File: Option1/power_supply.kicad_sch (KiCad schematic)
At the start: 36 parts, among them U201 U7812-500, U202 K7805-500R2_C909663, U203 SY8089AAAC, U204 SY8089AAAC

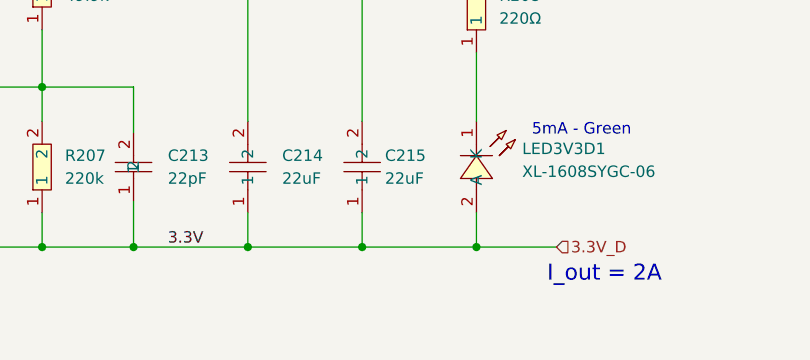
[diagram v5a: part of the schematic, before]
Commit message: 3V3 für Display hinzugefügt und gelayoutet, Brücke zwischen Display und Std 3V3 hinzugefügt in Schaltplan und Platine
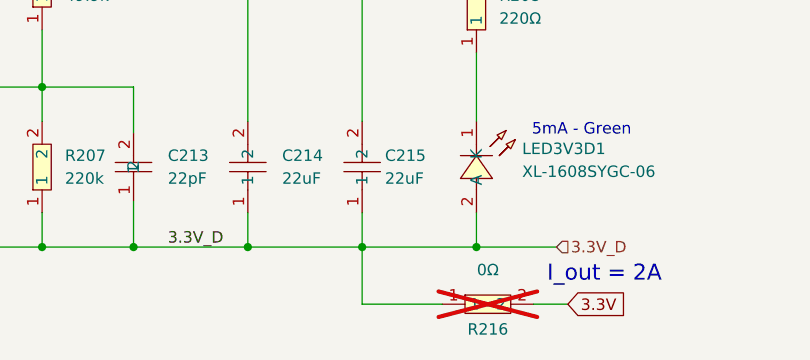
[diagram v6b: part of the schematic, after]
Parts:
- added R216: 0Ω, easyeda2kicad:R0603, symbol easyeda2kicad:0603WAF0000T5E
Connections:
- net 3.3V: now also R216.2; no longer C213.1, C214.1, C215.1, L202.2, LED3V3D1.2 (A), R207.1
- new net 3.3V_D: C213.1, C214.1, C215.1, L202.2, LED3V3D1.2 (A), R207.1, R216.1
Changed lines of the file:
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@@
+	(wire
+		(pts
+			(xy 236.22 116.84) (xy 227.33 116.84)
+		)
+		(stroke
+			(width 0)
+			(type default)
+		)
+	)
 	(wire
 		(pts
@@
 	(wire
 		(pts
+			(xy 227.33 116.84) (xy 227.33 110.49)
+		)
+		(stroke
+			(width 0)
+			(type default)
+		)
+	)
+	(wire
+		(pts
 			(xy 227.33 59.69) (xy 240.03 59.69)
 		)
@@
 		(pts
 			(xy 86.36 77.47) (xy 93.98 77.47)
+		)
+		(stroke
+			(width 0)
+			(type default)
+		)
+	)
+	(wire
+		(pts
+			(xy 246.38 116.84) (xy 250.19 116.84)
 		)
 		(stroke
@@
 		)
 	)
-	(label "3.3V"
+	(label "3.3V_D"
 		(at 205.74 110.49 0)
 		(effects
@@
 		(property "Intersheetrefs" "${INTERSHEET_REFS}"
 			(at 138.9357 57.15 0)
+			(effects
+				(font
+					(size 1.27 1.27)
+				)
+				(justify left)
+				(hide yes)
+			)
+		)
+	)
+	(global_label "3.3V"
+		(shape input)
+		(at 250.19 116.84 0)
+		(fields_autoplaced yes)
+		(effects
+			(font
+				(size 1.27 1.27)
+			)
+			(justify left)
+		)
+		(property "Intersheetrefs" "${INTERSHEET_REFS}"
+			(at 257.2876 116.84 0)
 			(effects
 				(font
@@
 					(unit 1)
 				)
+			)
+		)
+	)
+	(symbol
+		(lib_id "easyeda2kicad:0603WAF0000T5E")
+		(at 241.3 116.84 0)
+		(unit 1)
+		(exclude_from_sim no)
+		(in_bom no)
+		(on_board yes)
+		(dnp yes)
+		(property "Reference" "R216"
+			(at 241.3 119.634 0)
+			(effects
+				(font
+					(size 1.27 1.27)
+				)
+			)
+		)
+		(property "Value" "0Ω"
+			(at 241.3 113.03 0)
+			(effects
+				(font
+					(size 1.27 1.27)
+				)
+			)
+		)
+		(property "Footprint" "easyeda2kicad:R0603"
+			(at 241.3 124.46 0)
+			(effects
+				(font
+					(size 1.27 1.27)
+				)
+				(hide yes)
+			)
+		)
+		(property "Datasheet" "https://lcsc.com/product-detail/Chip-Resistor-Surface-Mount-UniOhm_0R-0R0-1_C21189.html"
+			(at 241.3 127 0)
+			(effects
+				(font
+					(size 1.27 1.27)
+				)
+				(hide yes)
+			)
+		)
+		(property "Description" ""
+			(at 241.3 116.84 0)
+			(effects
+				(font
+					(size 1.27 1.27)
+				)
+				(hide yes)
+			)
+		)
+		(property "LCSC Part" "C21189"
+			(at 241.3 129.54 0)
+			(effects
+				(font
+					(size 1.27 1.27)
+				)
+				(hide yes)
+			)
+		)
+		(pin "1"
+		)
+		(pin "2"
+		)
+		(instances
+			(project ""
+				(path "/b9e5f262-9648-4b79-bdd1-af888b822329/ff0aab3a-6ec2-4a6b-b0bf-5e79396b738a"
+					(reference "R216")
+					(unit 1)
+				)

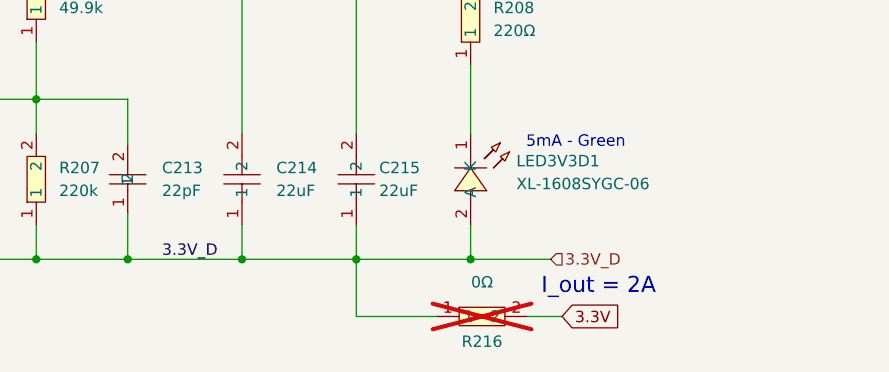
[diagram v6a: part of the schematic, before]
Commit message: GND polygon hinzugefügt, unverbundene Pads verknüpft, 0 Ohm Widerstand für Display Strohmversorgung hinzugefügt
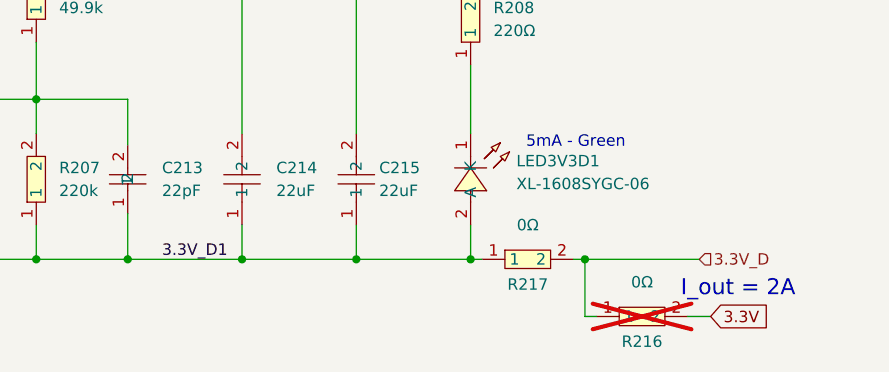
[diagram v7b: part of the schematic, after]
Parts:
- added R217: 0Ω, easyeda2kicad:R0603, symbol easyeda2kicad:0603WAF0000T5E
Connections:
- net 3.3V_D: now also R217.2; no longer C213.1, C214.1, C215.1, L202.2, LED3V3D1.2 (A), R207.1
- new net 3.3V_D1: C213.1, C214.1, C215.1, L202.2, LED3V3D1.2 (A), R207.1, R217.1
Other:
- moved on the sheet: R216
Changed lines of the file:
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@@
 	(text "I_out = 2A"
 		(exclude_from_sim no)
-		(at 254.254 113.538 0)
+		(at 269.748 113.792 0)
 		(effects
 			(font
@@
 	)
 	(junction
+		(at 252.73 110.49)
+		(diameter 0)
+		(color 0 0 0 0)
+	)
+	(junction
 		(at 201.93 59.69)
 		(diameter 0)
@@
 	(wire
 		(pts
-			(xy 236.22 116.84) (xy 227.33 116.84)
-		)
-		(stroke
-			(width 0)
-			(type default)
-		)
-	)
-	(wire
-		(pts
 			(xy 132.08 53.34) (xy 129.54 53.34)
 		)
@@
 	(wire
 		(pts
+			(xy 254 116.84) (xy 252.73 116.84)
+		)
+		(stroke
+			(width 0)
+			(type default)
+		)
+	)
+	(wire
+		(pts
 			(xy 181.61 92.71) (xy 191.77 92.71)
 		)
@@
 	(wire
 		(pts
+			(xy 252.73 110.49) (xy 265.43 110.49)
+		)
+		(stroke
+			(width 0)
+			(type default)
+		)
+	)
+	(wire
+		(pts
 			(xy 240.03 106.68) (xy 240.03 110.49)
 		)
@@
 	(wire
 		(pts
-			(xy 106.68 25.4) (xy 111.76 25.4)
+			(xy 251.46 110.49) (xy 252.73 110.49)
 		)
 		(stroke
@@
 	(wire
 		(pts
-			(xy 50.8 77.47) (xy 50.8 73.66)
+			(xy 106.68 25.4) (xy 111.76 25.4)
 		)
 		(stroke
@@
 	(wire
 		(pts
-			(xy 227.33 116.84) (xy 227.33 110.49)
+			(xy 50.8 77.47) (xy 50.8 73.66)
 		)
 		(stroke
@@
 	(wire
 		(pts
+			(xy 252.73 116.84) (xy 252.73 110.49)
+		)
+		(stroke
+			(width 0)
+			(type default)
+		)
+	)
+	(wire
+		(pts
 			(xy 106.68 25.4) (xy 106.68 36.83)
 		)
@@
 	(wire
 		(pts
-			(xy 240.03 110.49) (xy 248.92 110.49)
+			(xy 240.03 110.49) (xy 241.3 110.49)
 		)
 		(stroke
@@
 	(wire
 		(pts
-			(xy 246.38 116.84) (xy 250.19 116.84)
+			(xy 264.16 116.84) (xy 266.7 116.84)
 		)
 		(stroke
@@
 		)
 	)
-	(label "3.3V_D"
+	(label "3.3V_D1"
 		(at 205.74 110.49 0)
 		(effects
@@
 	(global_label "3.3V"
 		(shape input)
-		(at 250.19 116.84 0)
+		(at 266.7 116.84 0)
 		(fields_autoplaced yes)
 		(effects
@@
 		)
 		(property "Intersheetrefs" "${INTERSHEET_REFS}"
-			(at 257.2876 116.84 0)
+			(at 273.7976 116.84 0)
 			(effects
 				(font
@@
 	(hierarchical_label "3.3V_D"
 		(shape input)
-		(at 248.92 110.49 0)
+		(at 265.43 110.49 0)
 		(effects
 			(font
@@
 	(symbol
 		(lib_id "easyeda2kicad:0603WAF0000T5E")
-		(at 241.3 116.84 0)
+		(at 259.08 116.84 0)
 		(unit 1)
 		(exclude_from_sim no)
@@
 		(dnp yes)
 		(property "Reference" "R216"
-			(at 241.3 119.634 0)
+			(at 259.08 119.634 0)
 			(effects
 				(font
@@
 		)
 		(property "Value" "0Ω"
-			(at 241.3 113.03 0)
+			(at 259.08 113.03 0)
 			(effects
 				(font
@@
 		)
 		(property "Footprint" "easyeda2kicad:R0603"
-			(at 241.3 124.46 0)
+			(at 259.08 124.46 0)
 			(effects
 				(font
@@
 		)
 		(property "Datasheet" "https://lcsc.com/product-detail/Chip-Resistor-Surface-Mount-UniOhm_0R-0R0-1_C21189.html"
-			(at 241.3 127 0)
+			(at 259.08 127 0)
 			(effects
 				(font
@@
 		)
 		(property "Description" ""
-			(at 241.3 116.84 0)
+			(at 259.08 116.84 0)
 			(effects
 				(font
@@
 		)
 		(property "LCSC Part" "C21189"
-			(at 241.3 129.54 0)
+			(at 259.08 129.54 0)
 			(effects
 				(font
@@
 					(unit 1)
 				)
+			)
+		)
+	)
+	(symbol
+		(lib_id "easyeda2kicad:0603WAF0000T5E")
+		(at 246.38 110.49 0)
+		(unit 1)
+		(exclude_from_sim no)
+		(in_bom yes)
+		(on_board yes)
+		(dnp no)
+		(property "Reference" "R217"
+			(at 246.38 113.284 0)
+			(effects
+				(font
+					(size 1.27 1.27)
+				)
+			)
+		)
+		(property "Value" "0Ω"
+			(at 246.38 106.68 0)
+			(effects
+				(font
+					(size 1.27 1.27)
+				)
+			)
+		)
+		(property "Footprint" "easyeda2kicad:R0603"
+			(at 246.38 118.11 0)
+			(effects
+				(font
+					(size 1.27 1.27)
+				)
+				(hide yes)
+			)
+		)
+		(property "Datasheet" "https://lcsc.com/product-detail/Chip-Resistor-Surface-Mount-UniOhm_0R-0R0-1_C21189.html"
+			(at 246.38 120.65 0)
+			(effects
+				(font
+					(size 1.27 1.27)
+				)
+				(hide yes)
+			)
+		)
+		(property "Description" ""
+			(at 246.38 110.49 0)
+			(effects
+				(font
+					(size 1.27 1.27)
+				)
+				(hide yes)
+			)
+		)
+		(property "LCSC Part" "C21189"
+			(at 246.38 123.19 0)
+			(effects
+				(font
+					(size 1.27 1.27)
+				)
+				(hide yes)
+			)
+		)
+		(pin "1"
+		)
+		(pin "2"
+		)
+		(instances
+			(project "Option1"
+				(path "/b9e5f262-9648-4b79-bdd1-af888b822329/ff0aab3a-6ec2-4a6b-b0bf-5e79396b738a"
+					(reference "R217")
+					(unit 1)
+				)

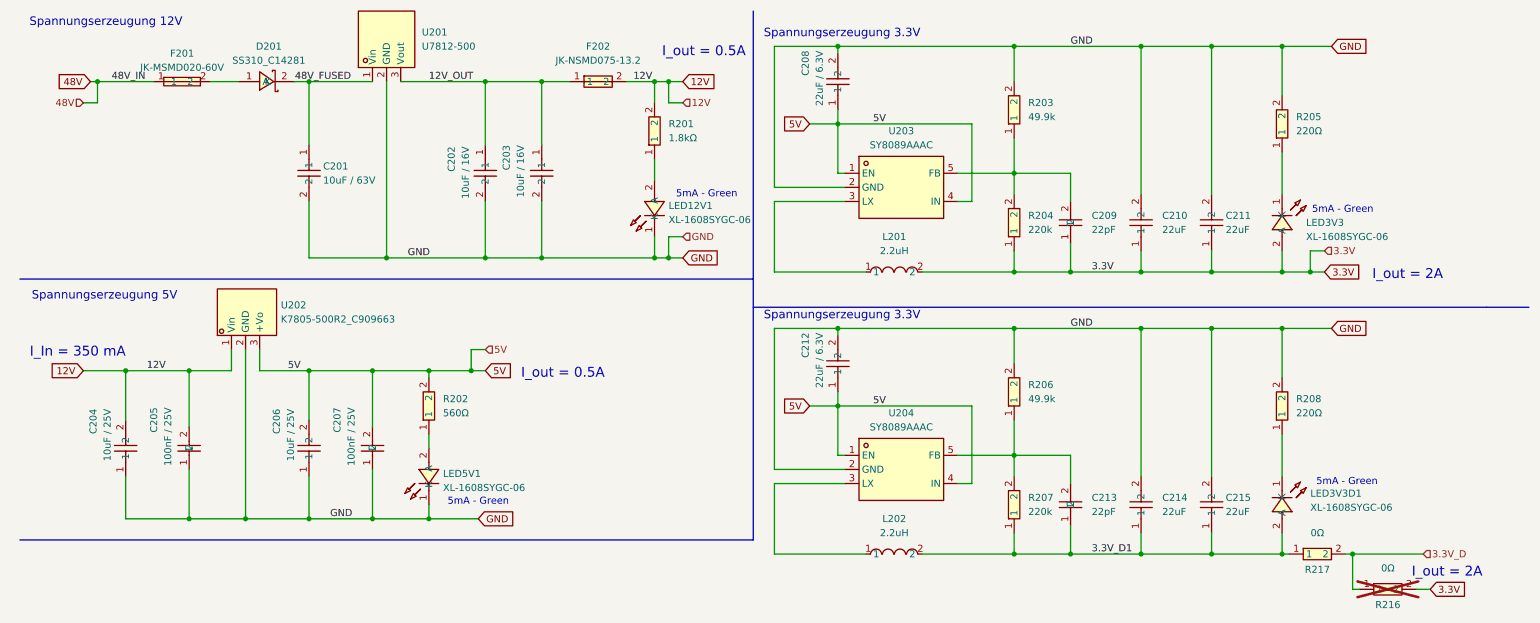
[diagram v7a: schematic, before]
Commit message: Kapitel über Schaltplan fortgesetzt, Fehler in Schaltplan korrigiert, DCDC getauscht, USB Schaltung angepasst, 3.3V Schaltung angepasst
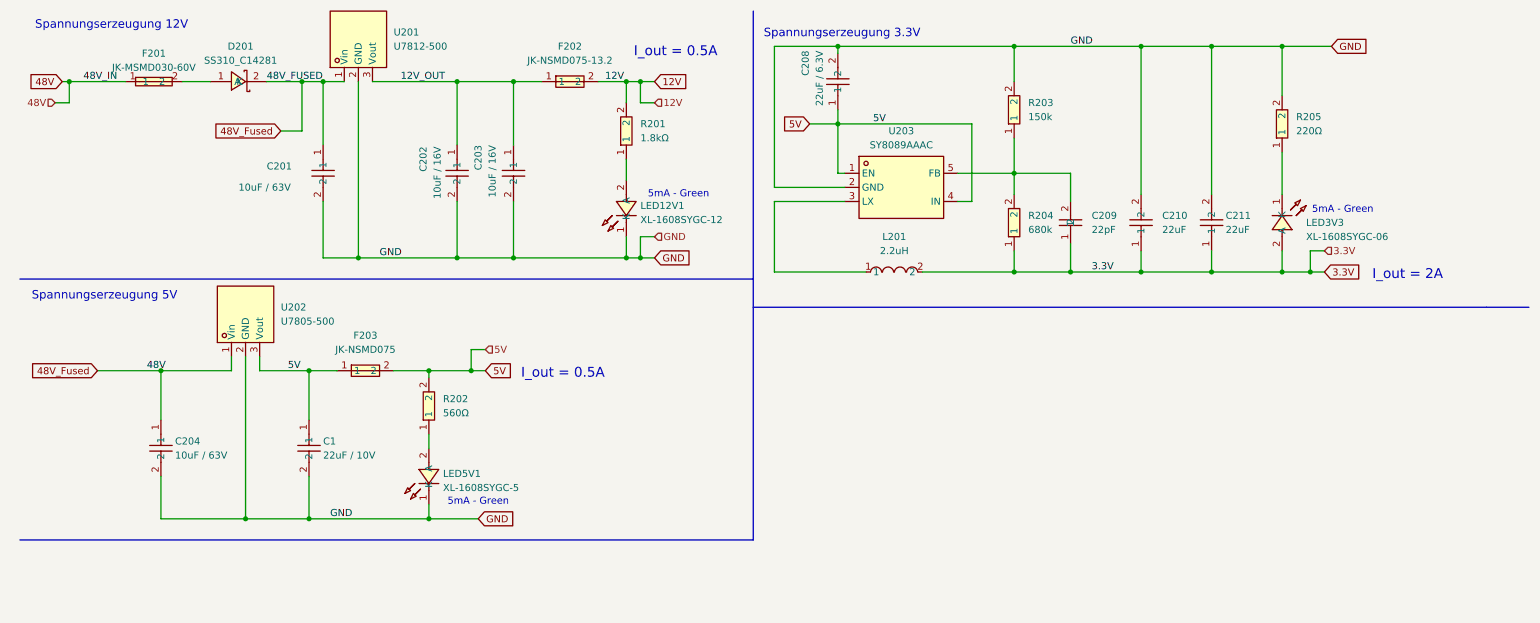
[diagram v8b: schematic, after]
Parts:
- removed C204, C206: 10uF / 25V, easyeda2kicad:C0805, symbol easyeda2kicad:CL21A106KAYNNNE
- removed C205, C207: 100nF / 25V, easyeda2kicad:C0603, symbol easyeda2kicad:CL10B104KA8NNNC
- removed C212: 22uF / 6.3V, easyeda2kicad:C0603, symbol easyeda2kicad:CL10A226MQ8NRNC
- removed C213: 22pF, easyeda2kicad:C0805, symbol easyeda2kicad:CL21C220JBANNNC
- removed C214, C215: 22uF, easyeda2kicad:C0805, symbol easyeda2kicad:CL21A226MAQNNNE
- removed L202: 2.2uH, easyeda2kicad:IND-SMD_L3.0-W3.0_NR3010, symbol easyeda2kicad:NR3015T2R2M
- removed LED3V3D1: XL-1608SYGC-06, easyeda2kicad:LED0603-RD_GREEN, symbol EasyEda2KiCad:XL-1608SYGC-06
- removed R203, R206: 49.9k, easyeda2kicad:R0603, symbol easyeda2kicad:0603WAF4992T5E
- removed R204, R207: 220k, easyeda2kicad:R0603, symbol easyeda2kicad:0603WAF2203T5E
- removed R208: 220Ω, easyeda2kicad:R0603, symbol EasyEda2KiCad:0603WAJ0221T5E
- removed R216, R217: 0Ω, easyeda2kicad:R0603, symbol easyeda2kicad:0603WAF0000T5E
- removed U202: K7805-500R2_C909663, easyeda2kicad:PWRM-TH_K78XX-500R3, symbol easyeda2kicad:K7805-500R2_C909663
- removed U204: SY8089AAAC, easyeda2kicad:SOT-23-5_L3.0-W1.7-P0.95-LS2.8-BR, symbol easyeda2kicad:SY8089AAAC
- added C1: 22uF / 10V, easyeda2kicad:C1210, symbol easyeda2kicad:GRM32ER71J106KA12L_C437568
- added C204: 10uF / 63V, easyeda2kicad:C1210, symbol easyeda2kicad:GRM32ER71J106KA12L_C437568
- added F203: JK-NSMD075, easyeda2kicad:F1206, symbol easyeda2kicad:JK-NSMD075-13.2
- added R203: 150k, easyeda2kicad:R0603, symbol easyeda2kicad:0603WAF1503T5E
- added R204: 680k, easyeda2kicad:R0603, symbol easyeda2kicad:0603WAJ0684T5E
- added U202: U7805-500, easyeda2kicad:PWRM-TH_3P-L11.6-W9.0-P2.54, symbol easyeda2kicad:U7805-500
- F201: value JK-MSMD020-60V -> JK-MSMD030-60V
- LED12V1: value XL-1608SYGC-06 -> XL-1608SYGC-12
- LED5V1: value XL-1608SYGC-06 -> XL-1608SYGC-5
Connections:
- net 48V_FUSED is gone; now on net 48V: C201.1, D201.2 (K), U201.1 (Vin)
- net 3.3V: now also R204.1
- net 48V: now also C204.1, U202.1 (Vin)
- net 5V: now also C1.1, F203.1, F203.2, U202.3 (Vout)
- net GND: now also C1.2, C204.2, R203.2, U202.2 (GND)
- net at C209.2, U203.5 (FB): now also R203.1, R204.2
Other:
- note removed: "I_In = 350 mA"
- moved on the sheet: C201, C202, C203, D201, F201, F202, LED12V1, R201, U201
